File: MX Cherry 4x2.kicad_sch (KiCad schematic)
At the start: 18 parts, among them J1 Conn_01x10_Pin, J2 Conn_01x10_Pin, SW1 SW_Push, SW2 SW_Push, SW3 SW_Push, SW4 SW_Push, SW5 SW_Push, SW6 SW_Push, SW7 SW_Push, SW8 SW_Push

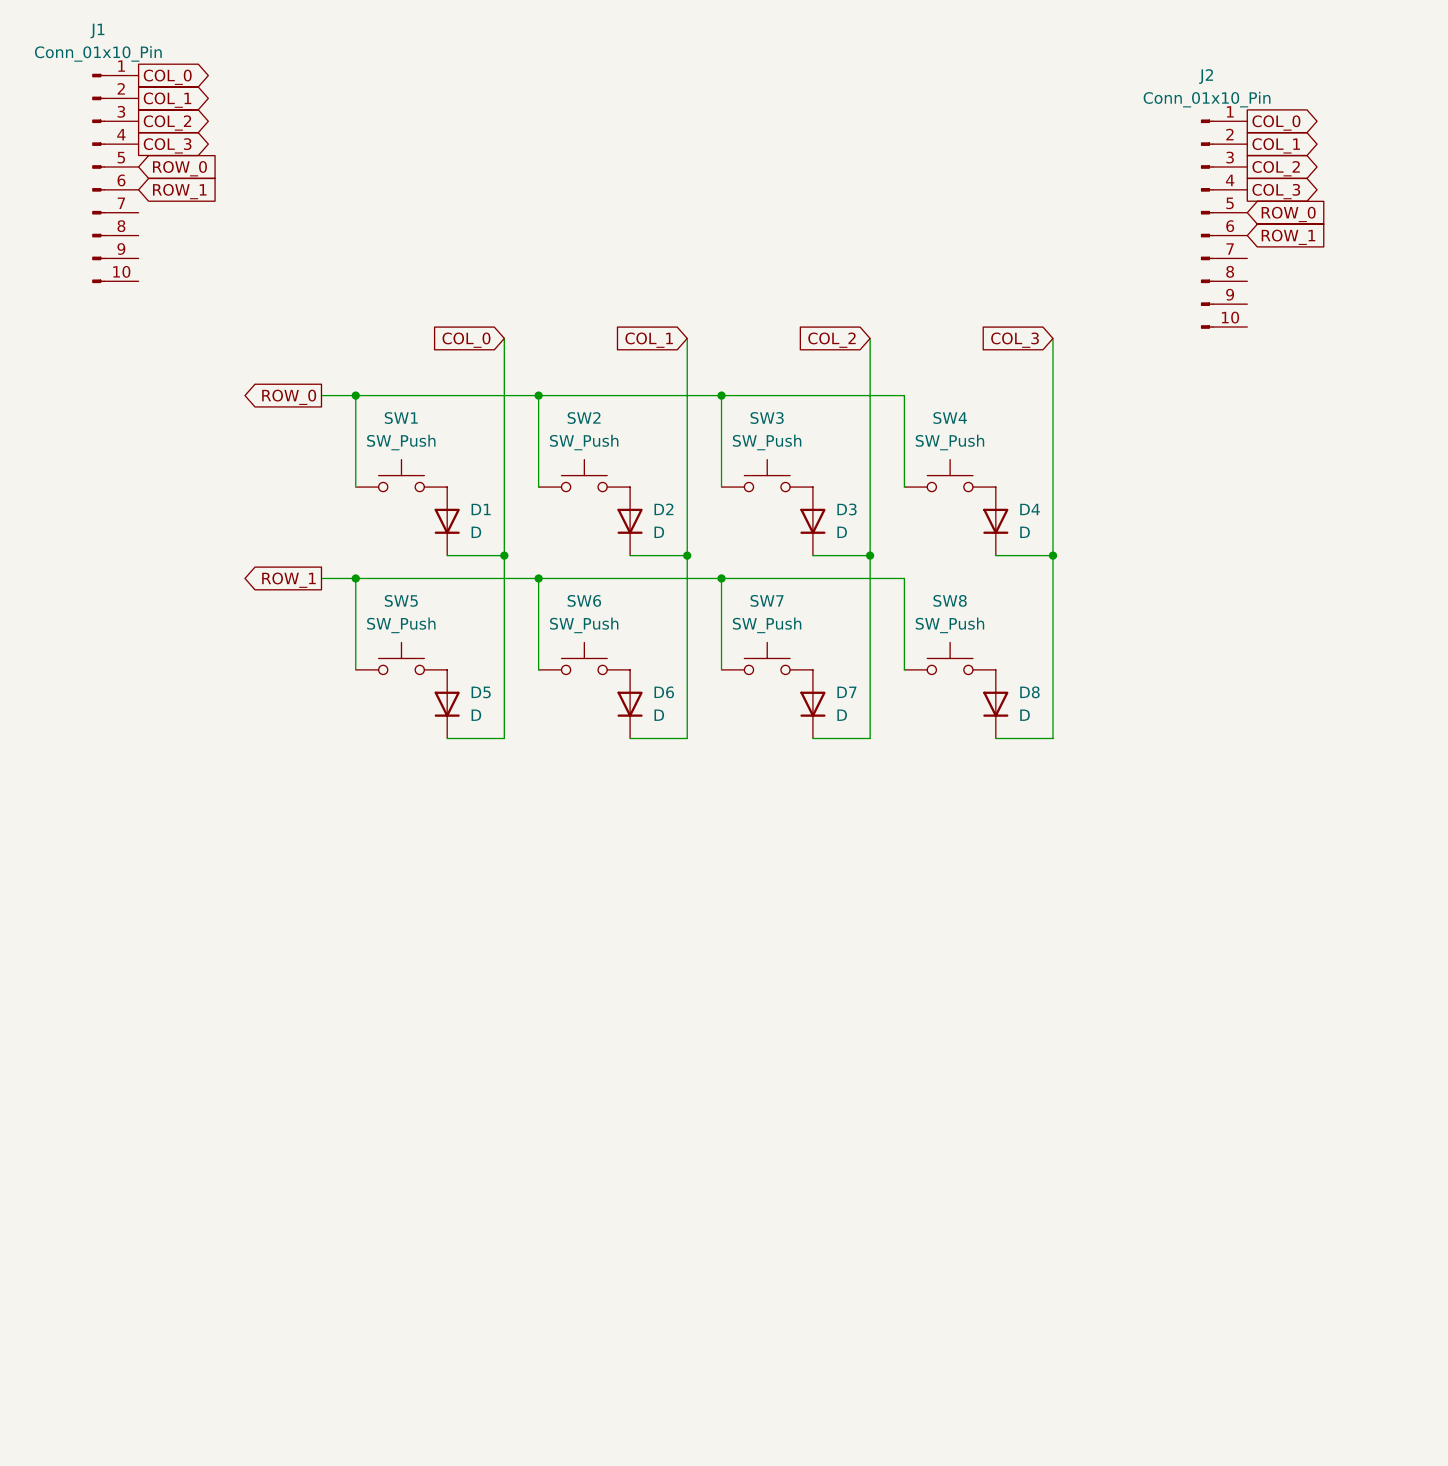
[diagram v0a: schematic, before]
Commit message: Add LEDs
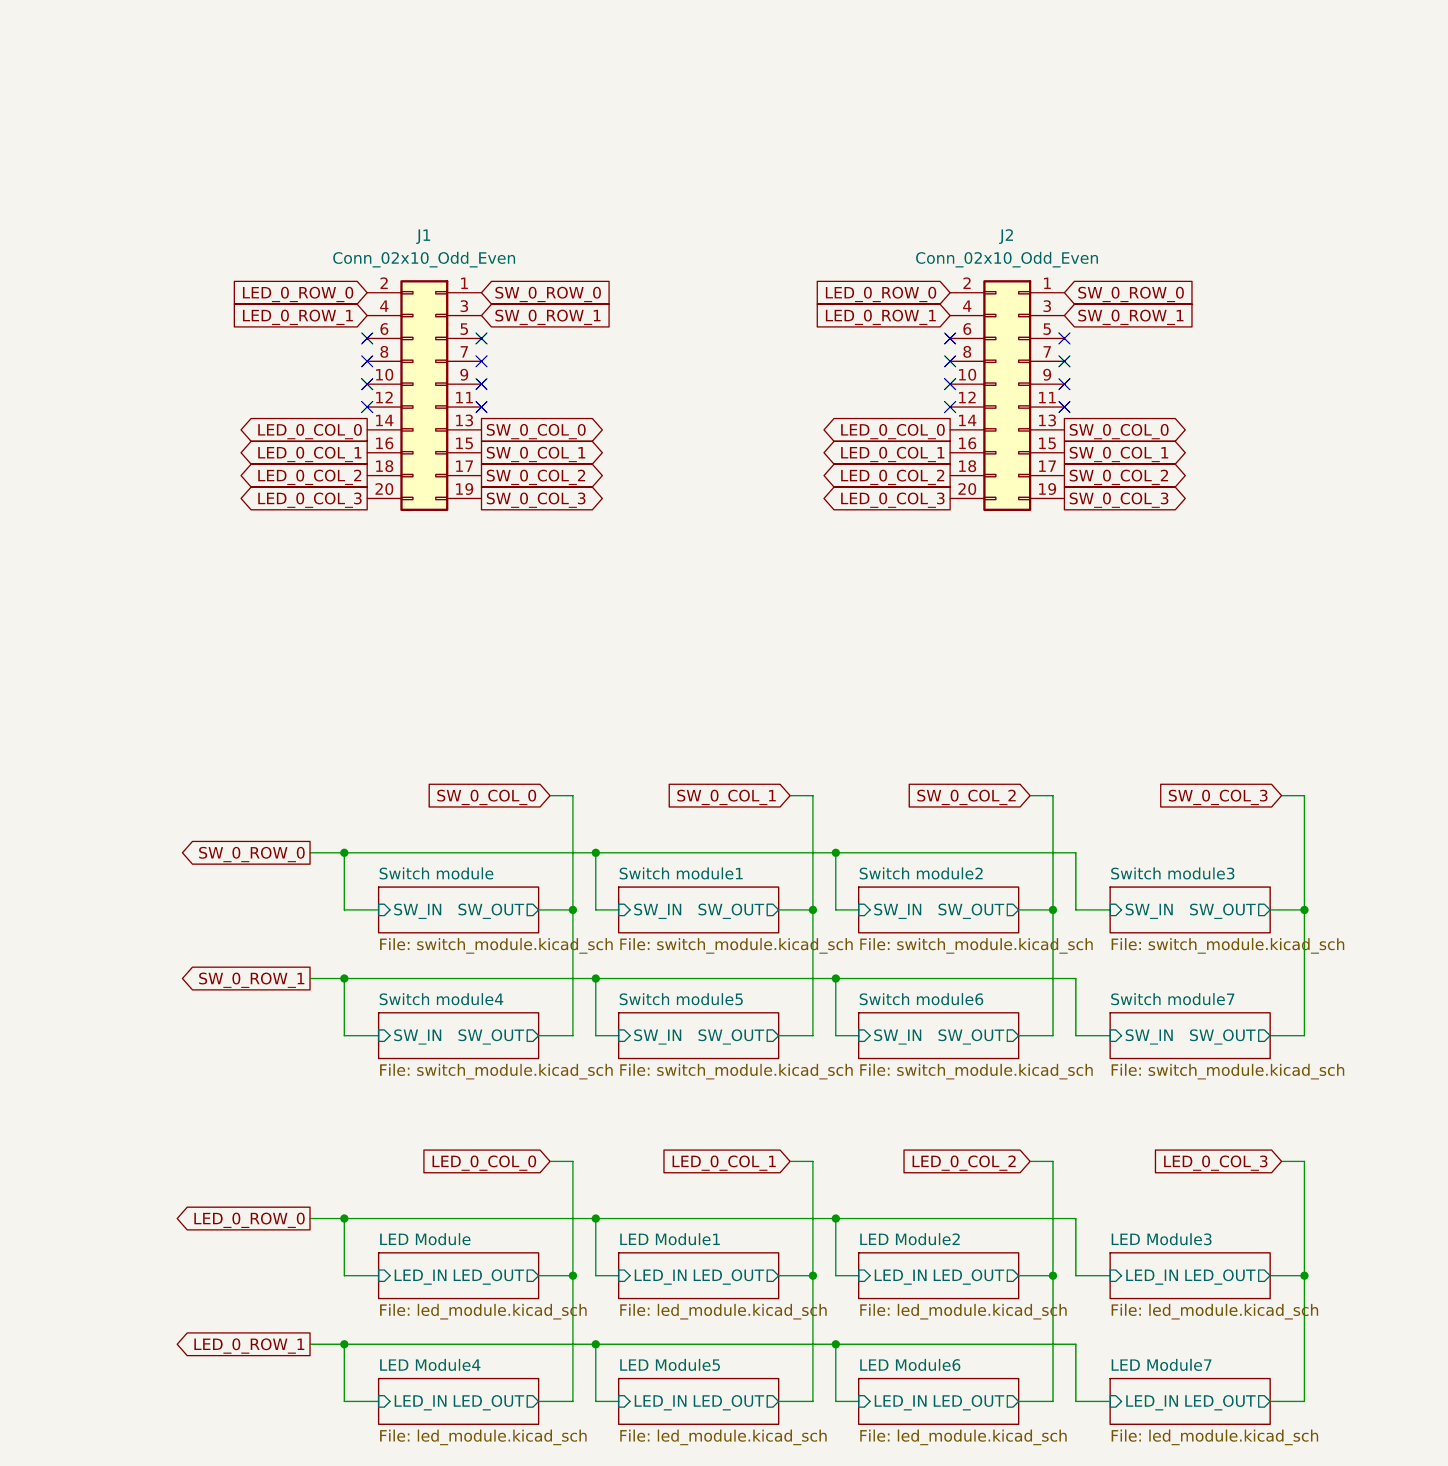
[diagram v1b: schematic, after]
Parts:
- removed D1, D2, D3, D4, D5, D6, D7, D8: D, Diode_THT:D_A-405_P7.62mm_Horizontal, symbol Device:D
- removed J1, J2: Conn_01x10_Pin, Connector_PinHeader_2.54mm:PinHeader_1x10_P2.54mm_Vertical, symbol Connector:Conn_01x10_Pin
- removed SW1, SW2, SW3, SW4, SW5, SW6, SW7, SW8: SW_Push, Button_Switch_Keyboard:SW_Cherry_MX_1.00u_PCB, symbol Switch:SW_Push
- added J1, J2: Conn_02x10_Odd_Even, Connector_PinSocket_2.54mm:PinSocket_2x10_P2.54mm_Vertical_SMD, symbol Connector_Generic:Conn_02x10_Odd_Even
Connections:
- new net LED_0_COL_0: J1.14 (Pin_14), J2.14 (Pin_14)
- new net LED_0_COL_1: J1.16 (Pin_16), J2.16 (Pin_16)
- new net LED_0_COL_2: J1.18 (Pin_18), J2.18 (Pin_18)
- new net LED_0_COL_3: J1.20 (Pin_20), J2.20 (Pin_20)
- new net LED_0_ROW_0: J1.2 (Pin_2), J2.2 (Pin_2)
- new net LED_0_ROW_1: J1.4 (Pin_4), J2.4 (Pin_4)
- new net SW_0_COL_0: J1.13 (Pin_13), J2.13 (Pin_13)
- new net SW_0_COL_1: J1.15 (Pin_15), J2.15 (Pin_15)
- new net SW_0_COL_2: J1.17 (Pin_17), J2.17 (Pin_17)
- new net SW_0_COL_3: J1.19 (Pin_19), J2.19 (Pin_19)
- new net SW_0_ROW_0: J1.1 (Pin_1), J2.1 (Pin_1)
- new net SW_0_ROW_1: J1.3 (Pin_3), J2.3 (Pin_3)
- no-connect marks 0 -> 16
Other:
- added sheet LED Module (led_module.kicad_sch)
- added sheet LED Module1 (led_module.kicad_sch)
- added sheet LED Module2 (led_module.kicad_sch)
- added sheet LED Module3 (led_module.kicad_sch)
- added sheet LED Module4 (led_module.kicad_sch)
- added sheet LED Module5 (led_module.kicad_sch)
- added sheet LED Module6 (led_module.kicad_sch)
- added sheet LED Module7 (led_module.kicad_sch)
- added sheet Switch module (switch_module.kicad_sch)
- added sheet Switch module1 (switch_module.kicad_sch)
- added sheet Switch module2 (switch_module.kicad_sch)
- added sheet Switch module3 (switch_module.kicad_sch)
- added sheet Switch module4 (switch_module.kicad_sch)
- added sheet Switch module5 (switch_module.kicad_sch)
- added sheet Switch module6 (switch_module.kicad_sch)
- added sheet Switch module7 (switch_module.kicad_sch)
